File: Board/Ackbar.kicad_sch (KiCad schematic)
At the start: 12 parts, among them J1 TOF, J2 GNSS, J3 HALL, J4 MOTOR, J5 PWR_IN, J6 EPD, U1 ESP32-S3 Pico, U2 VREG, U3 TMC2209, U4 SN74LVC1G04

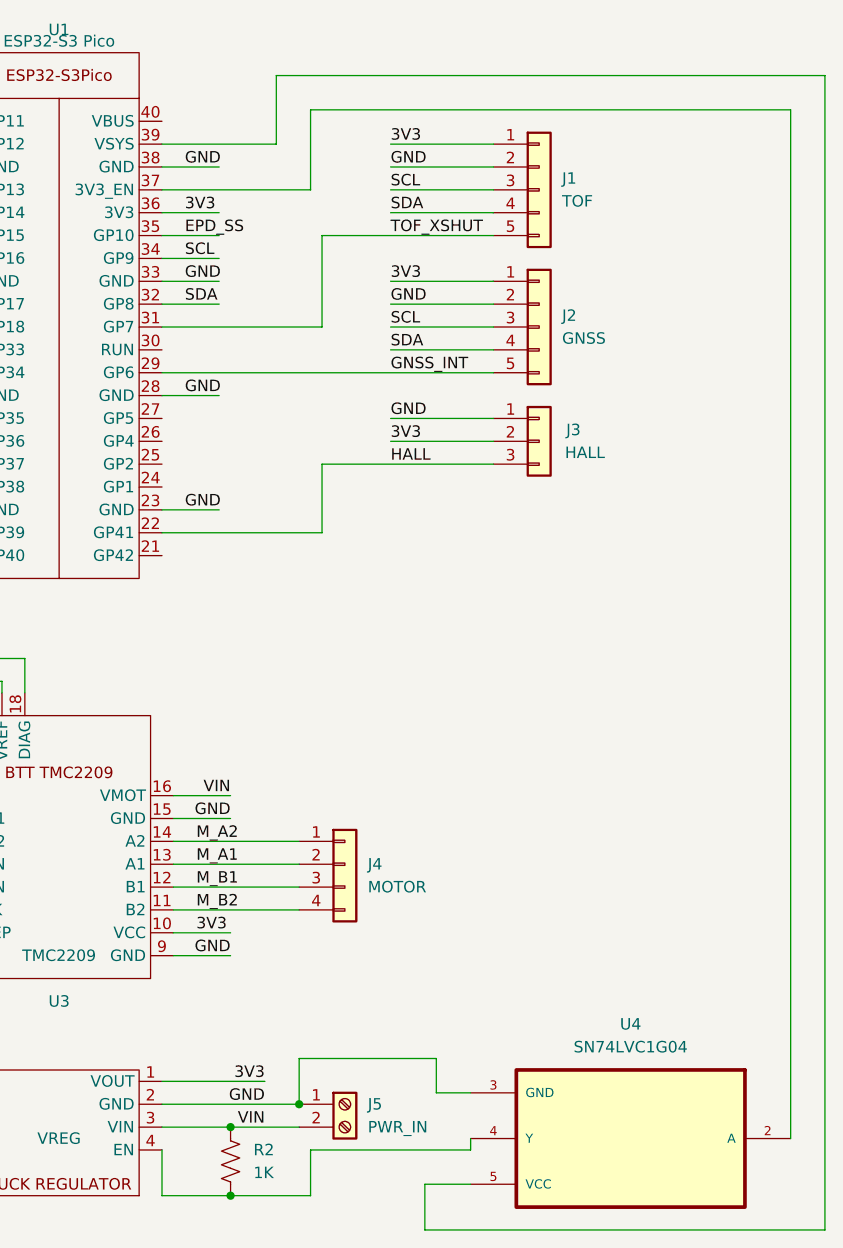
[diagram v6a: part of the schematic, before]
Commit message: Okay, you win, we're using the onboard regulator
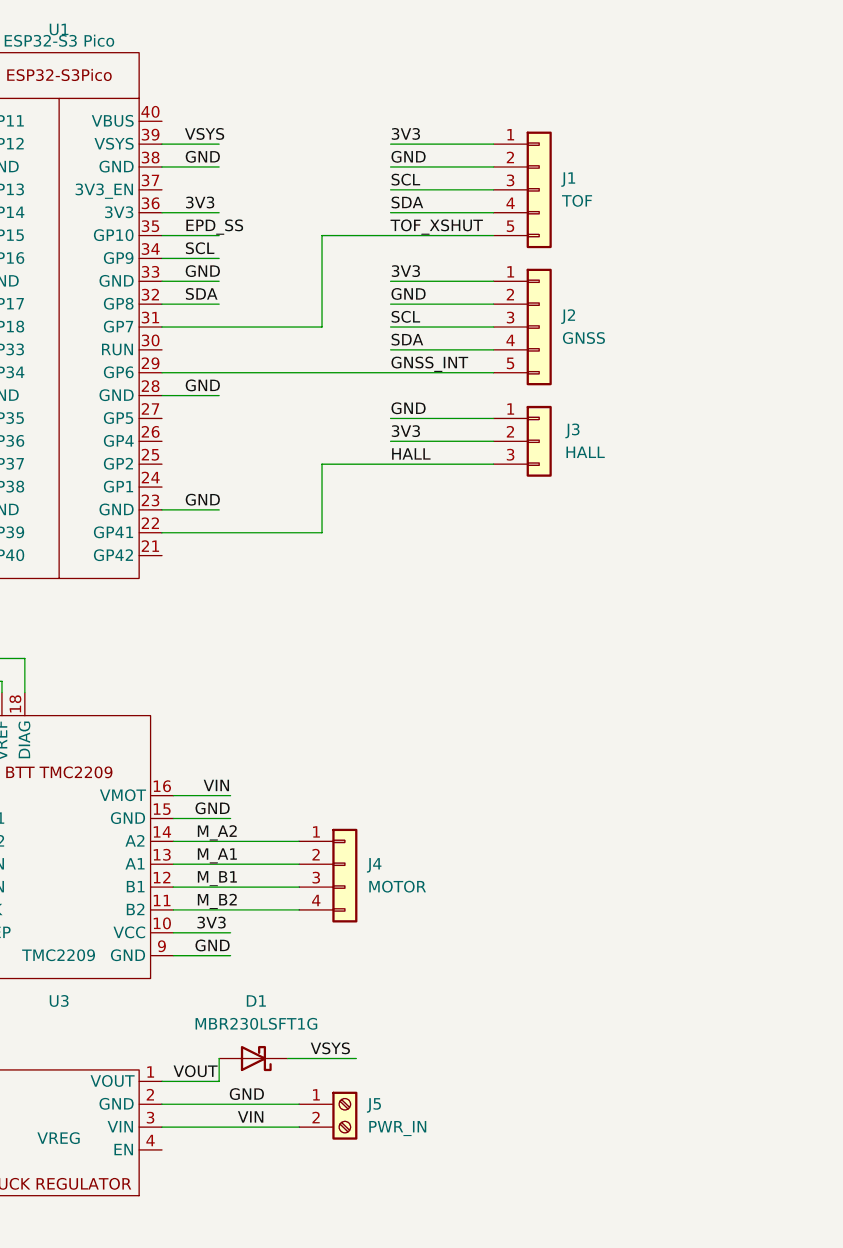
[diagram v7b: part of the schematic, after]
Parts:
- removed R2: 1K, Resistor_SMD:R_0805_2012Metric_Pad1.20x1.40mm_HandSolder, symbol Device:R_US
- removed U4: SN74LVC1G04, Ackbar:SOT95P280X145-5N, symbol Ackbar:SN74LVC1G04DCKR
- added D1: MBR230LSFT1G, Diode_SMD:D_SOD-123, symbol Diode:MBR340
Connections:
- net 3V3: no longer U2.1 (VOUT)
- net VSYS: now reaches U1.39 (VSYS)
- net VSYS: now also D1.1 (K)
- new net VOUT: D1.2 (A), U2.1 (VOUT)

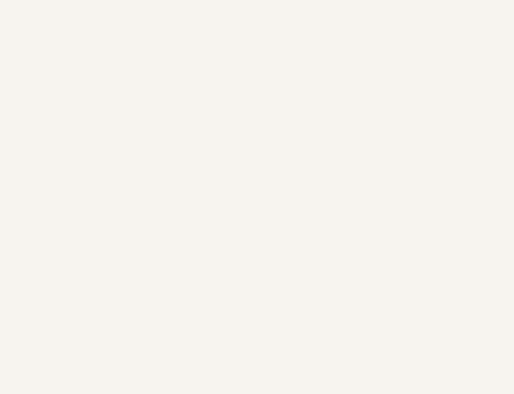
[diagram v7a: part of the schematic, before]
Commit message: Replace missing mounting holes
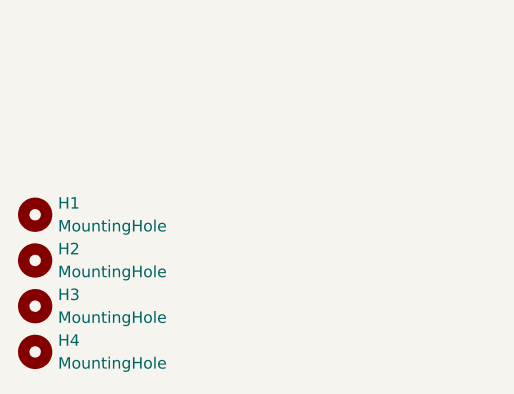
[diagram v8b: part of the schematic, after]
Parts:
- added H1, H2, H3, H4: MountingHole, MountingHole:MountingHole_3.2mm_M3, symbol Mechanical:MountingHole
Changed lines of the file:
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@@
+    )
+  )
+  (symbol (lib_id "Mechanical:MountingHole") (at 16.51 177.8 0) (unit 1)
+    (in_bom yes) (on_board yes) (dnp no) (fields_autoplaced)
+    (property "Reference" "H1" (at 19.05 176.53 0)
+      (effects (font (size 1.27 1.27)) (justify left))
+    )
+    (property "Value" "MountingHole" (at 19.05 179.07 0)
+      (effects (font (size 1.27 1.27)) (justify left))
+    )
+    (property "Footprint" "MountingHole:MountingHole_3.2mm_M3" (at 16.51 177.8 0)
+      (effects (font (size 1.27 1.27)) hide)
+    )
+    (property "Datasheet" "~" (at 16.51 177.8 0)
+      (effects (font (size 1.27 1.27)) hide)
+    )
+    (instances
+      (project "Ackbar"
+        (path "/10d22af5-0d05-45a6-b4a8-43aad0d497f4"
+          (reference "H1") (unit 1)
+        )
+      )
     )
   )
@@
     )
   )
+  (symbol (lib_id "Mechanical:MountingHole") (at 16.51 187.96 0) (unit 1)
+    (in_bom yes) (on_board yes) (dnp no) (fields_autoplaced)
+    (property "Reference" "H3" (at 19.05 186.69 0)
+      (effects (font (size 1.27 1.27)) (justify left))
+    )
+    (property "Value" "MountingHole" (at 19.05 189.23 0)
+      (effects (font (size 1.27 1.27)) (justify left))
+    )
+    (property "Footprint" "MountingHole:MountingHole_3.2mm_M3" (at 16.51 187.96 0)
+      (effects (font (size 1.27 1.27)) hide)
+    )
+    (property "Datasheet" "~" (at 16.51 187.96 0)
+      (effects (font (size 1.27 1.27)) hide)
+    )
+    (instances
+      (project "Ackbar"
+        (path "/10d22af5-0d05-45a6-b4a8-43aad0d497f4"
+          (reference "H3") (unit 1)
+        )
+      )
+    )
+  )
   (symbol (lib_id "SparkFun-Connector:Conn_01x04") (at 143.51 123.19 0) (unit 1)
     (in_bom yes) (on_board yes) (dnp no) (fields_autoplaced)
@@
         )
       )
+    )
+  )
+  (symbol (lib_id "Mechanical:MountingHole") (at 16.51 193.04 0) (unit 1)
+    (in_bom yes) (on_board yes) (dnp no) (fields_autoplaced)
+    (property "Reference" "H4" (at 19.05 191.77 0)
+      (effects (font (size 1.27 1.27)) (justify left))
+    )
+    (property "Value" "MountingHole" (at 19.05 194.31 0)
+      (effects (font (size 1.27 1.27)) (justify left))
+    )
+    (property "Footprint" "MountingHole:MountingHole_3.2mm_M3" (at 16.51 193.04 0)
+      (effects (font (size 1.27 1.27)) hide)
+    )
+    (property "Datasheet" "~" (at 16.51 193.04 0)
+      (effects (font (size 1.27 1.27)) hide)
+    )
+    (instances
+      (project "Ackbar"
+        (path "/10d22af5-0d05-45a6-b4a8-43aad0d497f4"
+          (reference "H4") (unit 1)
+        )
+      )
+    )
+  )
+  (symbol (lib_id "Mechanical:MountingHole") (at 16.51 182.88 0) (unit 1)
+    (in_bom yes) (on_board yes) (dnp no) (fields_autoplaced)
+    (property "Reference" "H2" (at 19.05 181.61 0)
+      (effects (font (size 1.27 1.27)) (justify left))
+    )
+    (property "Value" "MountingHole" (at 19.05 184.15 0)
+      (effects (font (size 1.27 1.27)) (justify left))
+    )
+    (property "Footprint" "MountingHole:MountingHole_3.2mm_M3" (at 16.51 182.88 0)
+      (effects (font (size 1.27 1.27)) hide)
+    )
+    (property "Datasheet" "~" (at 16.51 182.88 0)
+      (effects (font (size 1.27 1.27)) hide)
+    )
+    (instances
+      (project "Ackbar"
+        (path "/10d22af5-0d05-45a6-b4a8-43aad0d497f4"
+          (reference "H2") (unit 1)
+        )
+      )
